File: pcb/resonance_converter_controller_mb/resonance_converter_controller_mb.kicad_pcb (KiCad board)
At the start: 4 copper layers, 100 x 100 mm, 42 parts, among them J1 FX18-120P-0.8SV, J2 FX18-120P-0.8SV, J3 Conn_01x02, J4 FX18-120P-0.8SV, Q1 Q_NPN_BEC, Q2 Q_NPN_BEC, Q3 Q_PMOS_GDS, U1 PCF8574RGTR, U2 TL431D, U3 74LVC1G04

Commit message: Prep for autoroute
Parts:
- moved D1 0.73 mm to (183.2, 42.8)
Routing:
- net GND: track 55.3 -> 526.7 mm, vias 12 -> 174
- net I2C_EXT_SDA: track 0.00 -> 20.4 mm, vias 0 -> 3
- net OUT_SYNC_3-: track 0.00 -> 18.6 mm, vias 0 -> 3
- net OUT_SYNC_2-: track 0.00 -> 18.6 mm, vias 0 -> 3
- net DOCK_GPIO0: track 4.64 -> 23.2 mm, vias 0 -> 3
- net DOCK_LCD_MOSI: track 0.00 -> 18.6 mm, vias 0 -> 3
- net DOCK_GPIO2: track 0.00 -> 18.6 mm, vias 0 -> 3
- net OUT_SYNC_1-: track 0.00 -> 18.6 mm, vias 0 -> 3
- net ISENSE_2: track 0.00 -> 18.5 mm, vias 0 -> 3
- net HRTIM_FLT3: track 0.00 -> 18.5 mm, vias 0 -> 3
- net OCD_IN: track 0.00 -> 18.5 mm, vias 0 -> 3
- net DOCK_CTRL_RX: track 0.00 -> 18.5 mm, vias 0 -> 3
- net DOCK_LCD_RST: track 0.00 -> 18.5 mm, vias 0 -> 3
- net DOCK_ENCODER_CHA: track 0.00 -> 18.5 mm, vias 0 -> 3
- net ISENSE_3: track 0.00 -> 18.5 mm, vias 0 -> 3
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- added copper zone on In4.Cu, net GND
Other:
- copper layers 4 -> 6

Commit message: _mb board freerouted
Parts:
- added D7: D, Diode_SMD:D_SMA, F.Cu at (143.9, 127.6)
- added D8: D, Diode_SMD:D_SMA, F.Cu at (143.9, 131.2)
- added J5: Conn_01x04_MountingPin, Connector_JST:JST_SH_SM04B-SRSS-TB_1x04-1MP_P1.00mm_Horizontal, F.Cu at (135.4, 131.3)
- added J6: Conn_01x04_MountingPin, Connector_JST:JST_SH_SM04B-SRSS-TB_1x04-1MP_P1.00mm_Horizontal, F.Cu at (141.6, 137.7)
- moved D5 5.28 mm to (141.5, 123.3), turned to 90 degrees
- moved U2 3.60 mm to (137.0, 115.6)
- moved R58 3.60 mm to (138.7, 111.7)
- moved RV1 3.60 mm to (136.8, 123.3)
- moved Q1 1.59 mm to (143.1, 117.9)
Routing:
- net I2C_EXT_SDA: track 20.4 -> 192.5 mm, vias 3 -> 6
- net I2C_EXT_SCL: track 16.4 -> 187.6 mm, vias 3 -> 7
- net DOCK_CTRL_TX: track 14.3 -> 150.3 mm, vias 3 -> 4
- net DOCK_CTRL_RX: track 18.5 -> 152.7 mm, vias 3 -> 4
- net DOCK_GPIO0: track 23.2 -> 156.9 mm, vias 3 -> 6
- net GND: track 526.7 -> 616.3 mm, vias 174 -> 180
- net DOCK_LCD_BL: track 15.5 -> 102.1 mm, vias 3 -> 7
- net DOCK_GPIO7: track 15.6 -> 100.1 mm, vias 3 -> 4
- net DOCK_GPIO1: track 14.3 -> 94.8 mm, vias 3 -> 4
- net DOCK_ENCODER_CHB: track 15.6 -> 95.7 mm
- net VSENSE_IN: track 18.5 -> 98.4 mm
- net FAN_PWM: track 14.3 -> 94.1 mm
- net DOCK_LCD_RST: track 18.5 -> 98.0 mm
- net AUX_ADC: track 14.2 -> 92.6 mm
- net DOCK_GPIO2: track 18.6 -> 96.5 mm, vias 3 -> 5
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
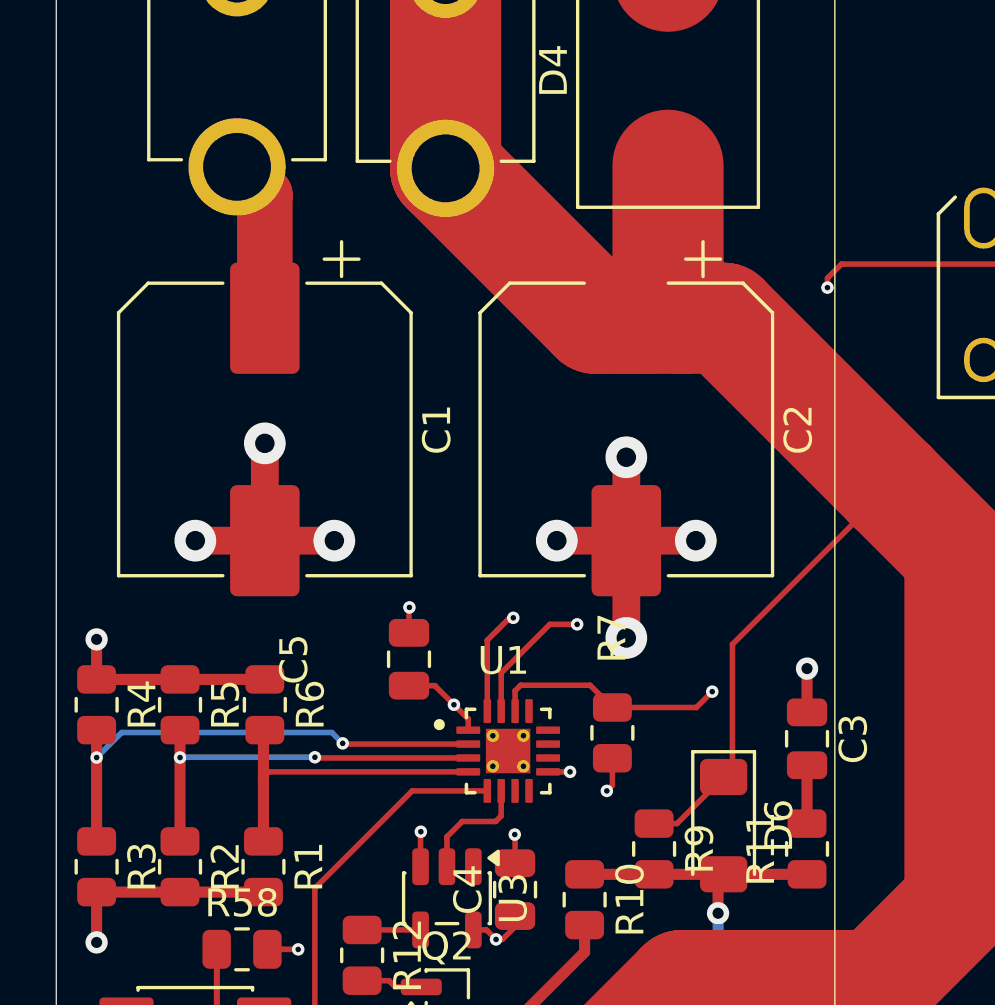
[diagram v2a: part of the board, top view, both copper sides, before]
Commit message: Add I2C line terminator
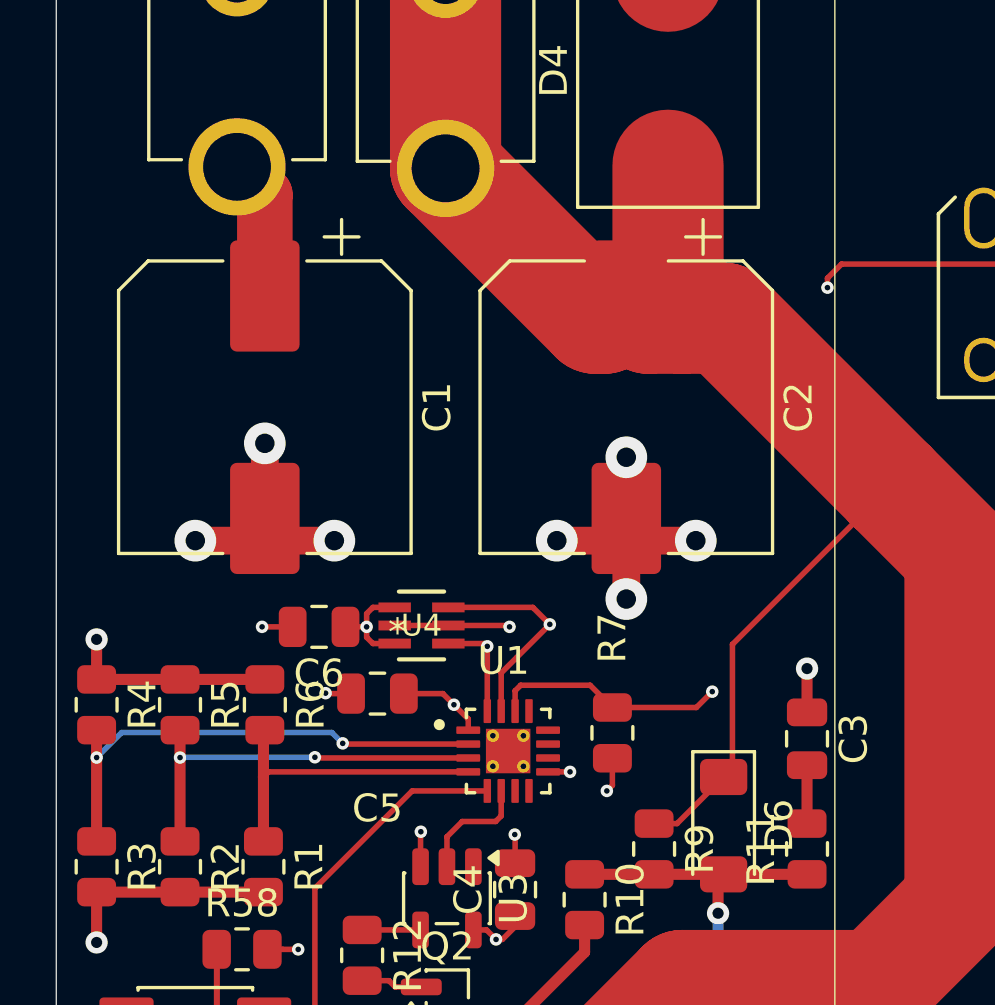
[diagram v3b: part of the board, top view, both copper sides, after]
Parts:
- added C6: C, Capacitor_SMD:C_0805_2012Metric, F.Cu at (141.4, 100.1)
- added U4: LTC4311CSC6, LTC4311CSC6:SC70-SC6, F.Cu at (145.1, 100.0)
- moved C5 1.68 mm to (143.6, 102.5), turned to 180 degrees
- moved C1 0.80 mm to (139.5, 92.2)
- moved C2 0.80 mm to (152.5, 92.2)
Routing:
- net GND: track 616.3 -> 620.7 mm, vias 180 -> 182
- net I2C_EXT_SCL: track 187.6 -> 191.1 mm
- net +3.3V: track 21.1 -> 24.2 mm, vias 5 -> 6
- net VDD: track 89.4 -> 90.1 mm

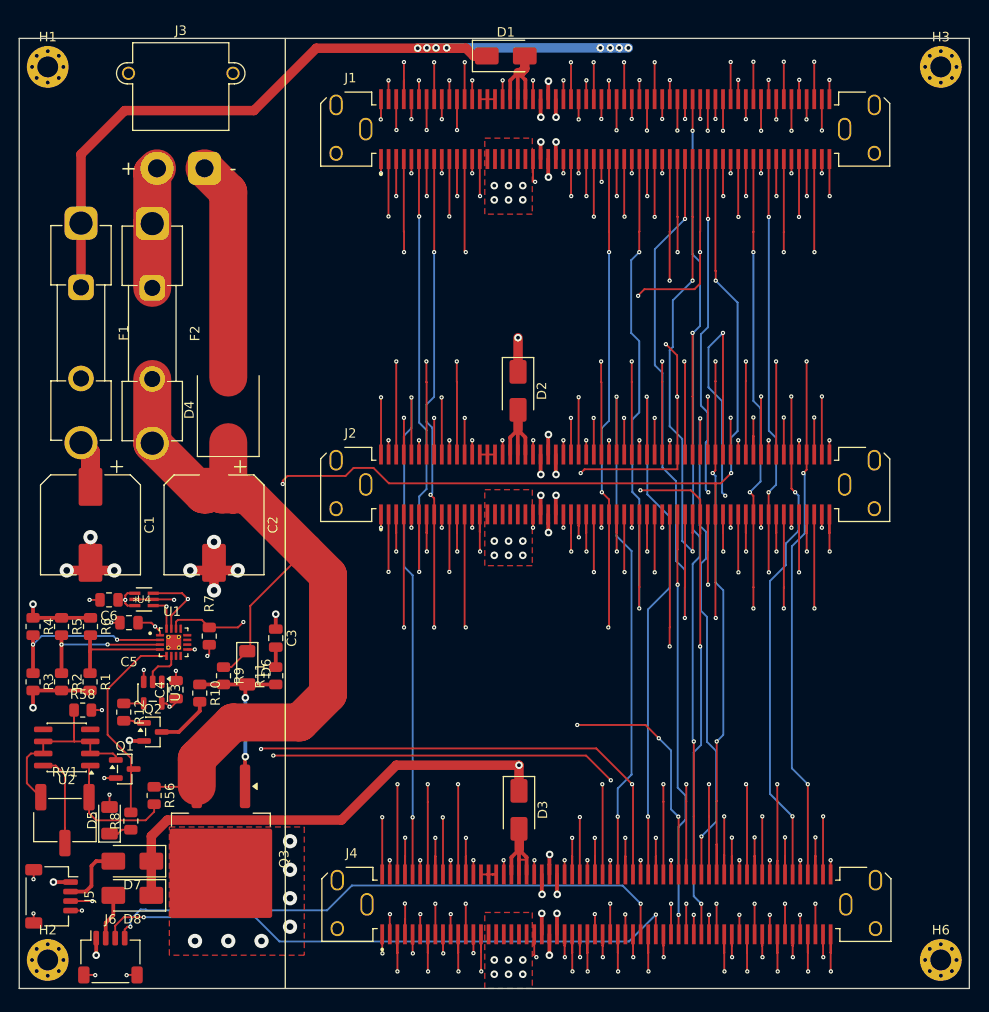
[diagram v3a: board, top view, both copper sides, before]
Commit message: Add 3.3v regulator and fix silkscreen
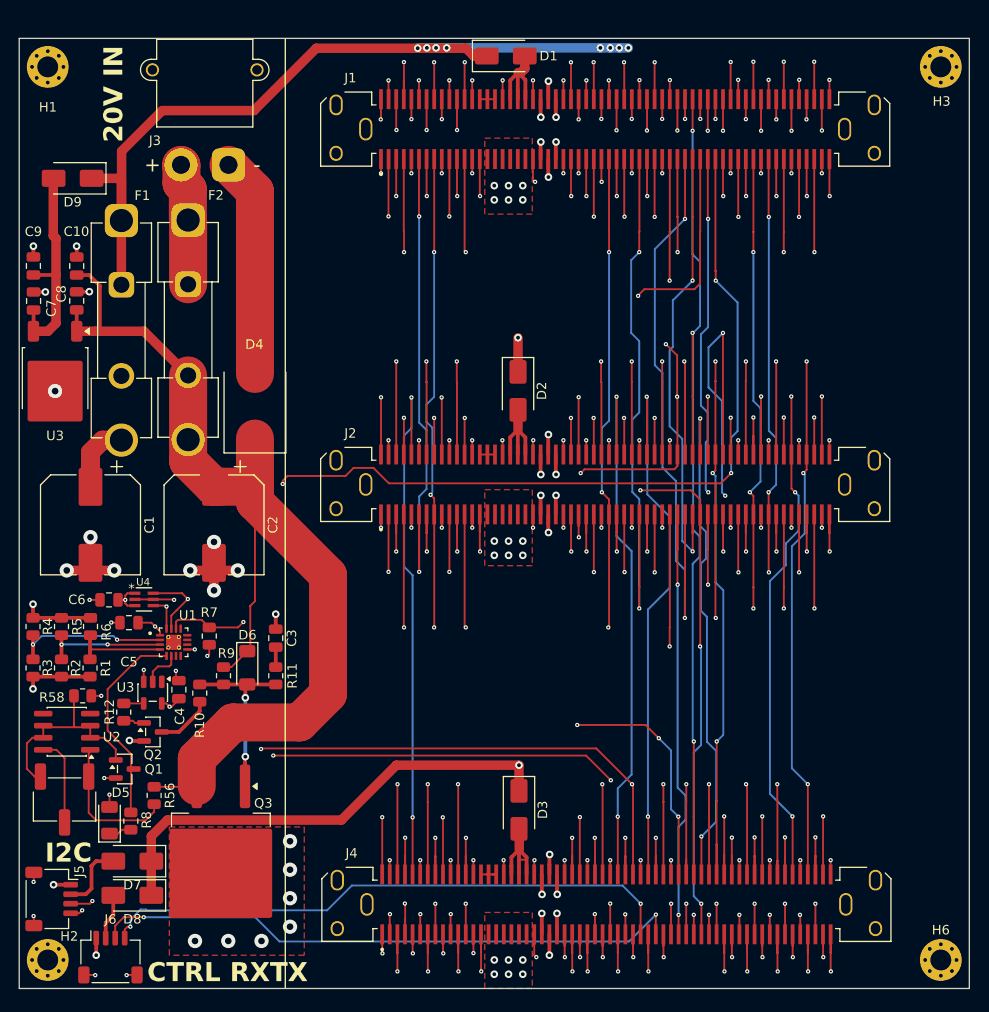
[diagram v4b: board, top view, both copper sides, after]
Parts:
- added C10: 10uF, Capacitor_SMD:C_0805_2012Metric, F.Cu at (138.1, 65.0)
- added C7: 100nF, Capacitor_SMD:C_0805_2012Metric, F.Cu at (133.5, 68.6)
- added C8: 100nF, Capacitor_SMD:C_0805_2012Metric, F.Cu at (138.1, 68.6)
- added C9: 10uF, Capacitor_SMD:C_0805_2012Metric, F.Cu at (133.5, 65.0)
- added D9: D, Diode_SMD:D_SMA, F.Cu at (137.6, 55.7)
- added U3: LP2950-3.3_TO252, Package_TO_SOT_SMD:TO-252-2, F.Cu at (135.8, 76.9)
- moved F1 4.26 mm to (142.8, 60.2)
- moved F2 3.79 mm to (149.8, 60.1)
- moved D4 2.84 mm to (156.8, 79.7)
- moved J3 2.55 mm to (154.0, 54.3)
- moved RV1 2.17 mm to (136.8, 121.1)
- moved U2 1.66 mm to (137.0, 114.0)
- moved R58 1.50 mm to (138.7, 110.2)
- moved R1 1.46 mm to (139.4, 107.3)
- moved R2 1.46 mm to (136.4, 107.3)
- moved R3 1.46 mm to (133.4, 107.3)
- moved C4 0.30 mm to (148.8, 109.5)
- moved J5 0.28 mm to (135.4, 131.6)
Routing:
- net VDD: track 90.1 -> 116.3 mm
- net Net-(D9-A): track 0.00 -> 22.7 mm
- net GND: track 620.7 -> 625.0 mm, vias 182 -> 187
- net EXT_VCC: track 158.3 -> 161.5 mm
- net +3.3V: track 24.2 -> 26.6 mm
- net Net-(U1-A2): track 11.5 -> 10.0 mm
- net Net-(U1-A1): track 14.4 -> 12.9 mm
- net Net-(U1-A0): track 17.9 -> 16.4 mm
- net Net-(Q1-B): track 23.6 -> 22.7 mm
- net DOCK_GPIO2: vias 5 -> 4
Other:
- board text added: "20V IN"
- board text added: "CTRL RXTX"
- board text added: "I2C"
